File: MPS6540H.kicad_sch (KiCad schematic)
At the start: 10 parts, among them U4 MPS6540H

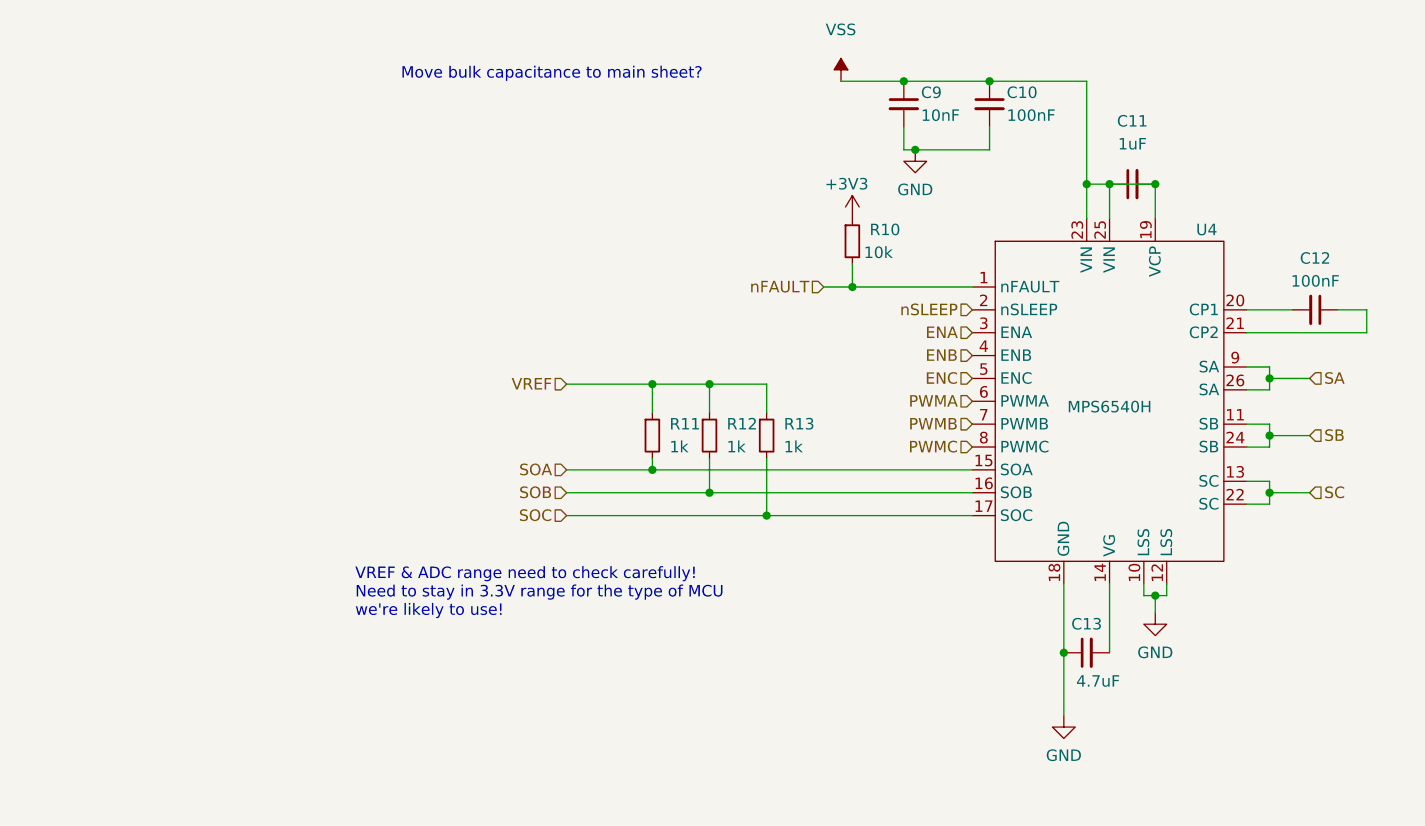
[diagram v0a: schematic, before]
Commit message: working on rosmo ESC, routing half done
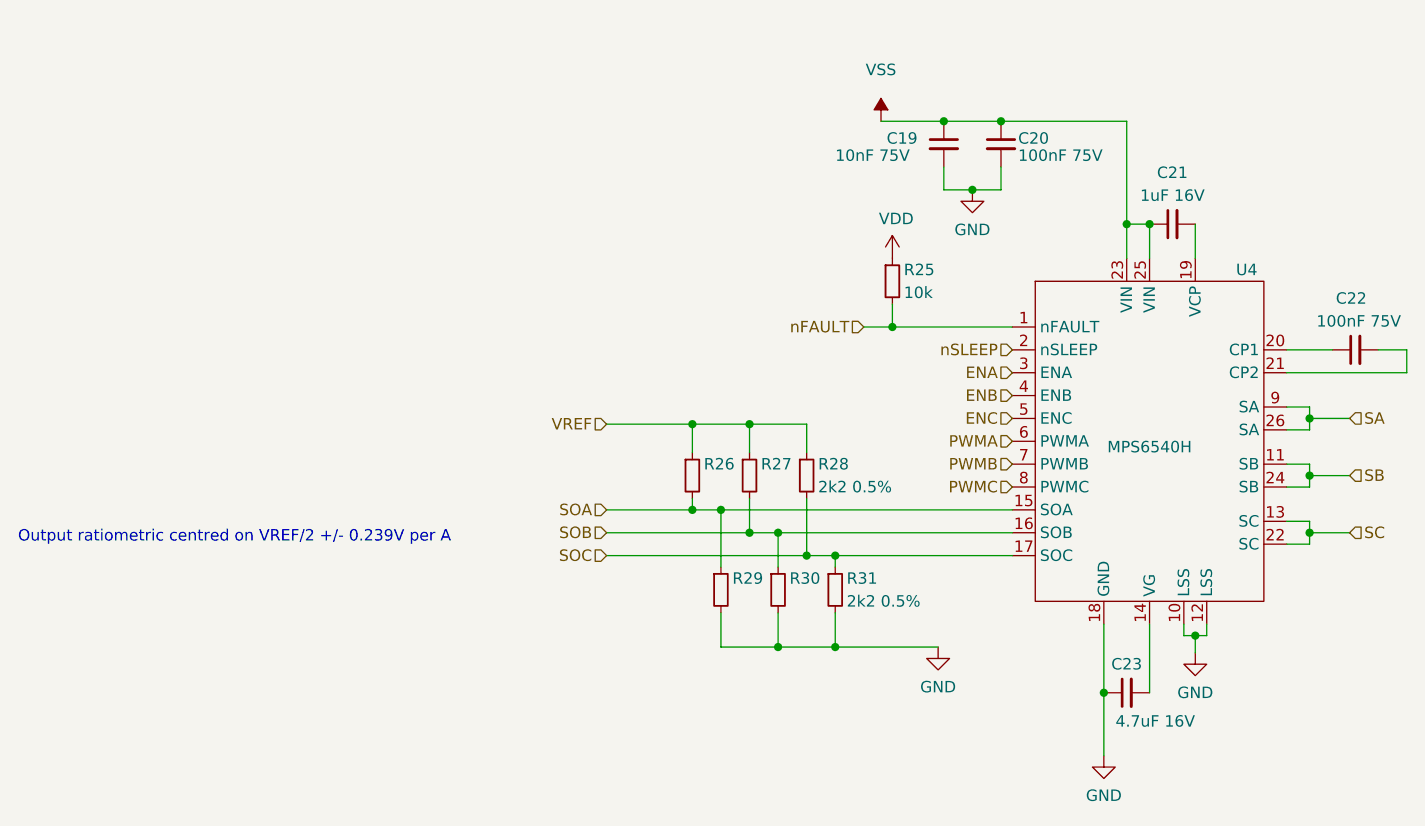
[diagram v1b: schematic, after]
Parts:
- removed C10, C12: 100nF, Capacitor_SMD:C_0805_2012Metric, symbol Device:C_Small
- removed C11: 1uF, Capacitor_SMD:C_0805_2012Metric, symbol Device:C_Small
- removed C13: 4.7uF, Capacitor_SMD:C_0805_2012Metric, symbol Device:C_Small
- removed C9: 10nF, Capacitor_SMD:C_0805_2012Metric, symbol Device:C_Small
- removed R10: 10k, Resistor_SMD:R_0402_1005Metric, symbol Device:R_Small
- removed R11, R12: 1k, Resistor_SMD:R_0402_1005Metric, symbol Device:R_Small
- removed R13: 1k, Capacitor_SMD:C_0805_2012Metric, symbol Device:R_Small
- added C19: 10nF 75V, Capacitor_SMD:C_0805_2012Metric, symbol Device:C_Small
- added C20, C22: 100nF 75V, Capacitor_SMD:C_0805_2012Metric, symbol Device:C_Small
- added C21: 1uF 16V, Capacitor_SMD:C_0603_1608Metric, symbol Device:C_Small
- added C23: 4.7uF 16V, Capacitor_SMD:C_0603_1608Metric, symbol Device:C_Small
- added R25: 10k, Resistor_SMD:R_0402_1005Metric, symbol Device:R_Small
- added R26, R27, R28, R29, R30, R31: 2k2 0.5%, Resistor_SMD:R_0402_1005Metric, symbol Device:R_Small
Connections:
- net GND: now also C19.2, C20.2, C23.1, R29.2, R30.2, R31.2
- net SOA: now also R26.2, R29.1
- net SOB: now also R27.2, R30.1
- net SOC: now also R28.2, R31.1
- net VREF: now also R26.1, R27.1, R28.1
- net VSS: now also C19.1, C20.1, C21.1; no longer U4.19 (VCP)
- net nFAULT: now also R25.2
- net at U4.14 (VG): now also C23.2
- net at U4.21 (CP2): now also C22.2
- net at U4.20 (CP1): now also C22.1
- new net: C21.2, U4.19 (VCP)
- new net VDD: R25.1
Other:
- note added: "Output ratiometric centred on VREF/2 +/- 0.239V per A"
- note removed: "Move bulk capacitance to main sheet?"
- note removed: "VREF & ADC range need to check carefully! Need to stay in 3.3V range for the type of MCU we're likely to use!"

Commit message: intial routing done
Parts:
- renumbered C19 to C14, C20 to C15, C21 to C16, C22 to C17, C23 to C18, R25 to R18, R26 to R19, R27 to R20, R28 to R21, R29 to R22, R30 to R23, R31 to R24, U4 to U3
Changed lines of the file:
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@@
   (symbol (lib_id "Device:R_Small") (at 114.3 97.79 0)
     (in_bom yes) (on_board yes)
-    (property "Reference" "R26" (id 0) (at 115.57 96.5199 0)
+    (property "Reference" "R19" (id 0) (at 115.57 96.5199 0)
       (effects (font (size 1.27 1.27)) (justify left))
     )
@@
   (symbol (lib_id "Device:R_Small") (at 117.475 110.49 0)
     (in_bom yes) (on_board yes)
-    (property "Reference" "R29" (id 0) (at 118.745 109.2199 0)
+    (property "Reference" "R22" (id 0) (at 118.745 109.2199 0)
       (effects (font (size 1.27 1.27)) (justify left))
     )
@@
   (symbol (lib_id "Device:R_Small") (at 120.65 97.79 0)
     (in_bom yes) (on_board yes)
-    (property "Reference" "R27" (id 0) (at 121.92 96.5199 0)
+    (property "Reference" "R20" (id 0) (at 121.92 96.5199 0)
       (effects (font (size 1.27 1.27)) (justify left))
     )
@@
   (symbol (lib_id "Device:R_Small") (at 123.825 110.49 0)
     (in_bom yes) (on_board yes)
-    (property "Reference" "R30" (id 0) (at 125.095 109.2199 0)
+    (property "Reference" "R23" (id 0) (at 125.095 109.2199 0)
       (effects (font (size 1.27 1.27)) (justify left))
     )
@@
   (symbol (lib_id "Device:R_Small") (at 127 97.79 0)
     (in_bom yes) (on_board yes)
-    (property "Reference" "R28" (id 0) (at 128.27 96.5199 0)
+    (property "Reference" "R21" (id 0) (at 128.27 96.5199 0)
       (effects (font (size 1.27 1.27)) (justify left))
     )
@@
   (symbol (lib_id "Device:R_Small") (at 130.175 110.49 0)
     (in_bom yes) (on_board yes)
-    (property "Reference" "R31" (id 0) (at 131.445 109.2199 0)
+    (property "Reference" "R24" (id 0) (at 131.445 109.2199 0)
       (effects (font (size 1.27 1.27)) (justify left))
     )
@@
   (symbol (lib_id "Device:R_Small") (at 136.525 76.2 0)
     (in_bom yes) (on_board yes)
-    (property "Reference" "R25" (id 0) (at 137.795 74.9299 0)
+    (property "Reference" "R18" (id 0) (at 137.795 74.9299 0)
       (effects (font (size 1.27 1.27)) (justify left))
     )
@@
   (symbol (lib_id "Device:C_Small") (at 142.24 60.96 0)
     (in_bom yes) (on_board yes)
-    (property "Reference" "C19" (id 0) (at 135.89 60.3249 0)
+    (property "Reference" "C14" (id 0) (at 135.89 60.3249 0)
       (effects (font (size 1.27 1.27)) (justify left))
     )
@@
   (symbol (lib_id "Device:C_Small") (at 148.59 60.96 0)
     (in_bom yes) (on_board yes)
-    (property "Reference" "C20" (id 0) (at 150.495 60.3249 0)
+    (property "Reference" "C15" (id 0) (at 150.495 60.3249 0)
       (effects (font (size 1.27 1.27)) (justify left))
     )
@@
   (symbol (lib_id "Device:C_Small") (at 162.56 121.92 90)
     (in_bom yes) (on_board yes)
-    (property "Reference" "C23" (id 0) (at 162.56 118.745 90))
+    (property "Reference" "C18" (id 0) (at 162.56 118.745 90))
     (property "Value" "4.7uF 16V" (id 1) (at 165.735 125.095 90))
     (property "Footprint" "Capacitor_SMD:C_0603_1608Metric" (id 2) (at 162.56 121.92 0)
@@
   (symbol (lib_id "Device:C_Small") (at 167.64 69.85 90)
     (in_bom yes) (on_board yes)
-    (property "Reference" "C21" (id 0) (at 167.64 64.135 90))
+    (property "Reference" "C16" (id 0) (at 167.64 64.135 90))
     (property "Value" "1uF 16V" (id 1) (at 167.64 66.675 90))
     (property "Footprint" "Capacitor_SMD:C_0603_1608Metric" (id 2) (at 167.64 69.85 0)
@@
   (symbol (lib_id "Device:C_Small") (at 187.96 83.82 90)
     (in_bom yes) (on_board yes)
-    (property "Reference" "C22" (id 0) (at 189.2299 78.105 90)
+    (property "Reference" "C17" (id 0) (at 189.2299 78.105 90)
       (effects (font (size 1.27 1.27)) (justify left))
     )
@@
   (symbol (lib_id "runger:MPS6540H") (at 165.1 93.98 0)
     (in_bom yes) (on_board yes)
-    (property "Reference" "U4" (id 0) (at 175.895 74.93 0))
+    (property "Reference" "U3" (id 0) (at 175.895 74.93 0))
     (property "Value" "MPS6540H" (id 1) (at 165.1 94.615 0))
     (property "Footprint" "runger:MPS6540H" (id 2) (at 149.86 81.28 0)

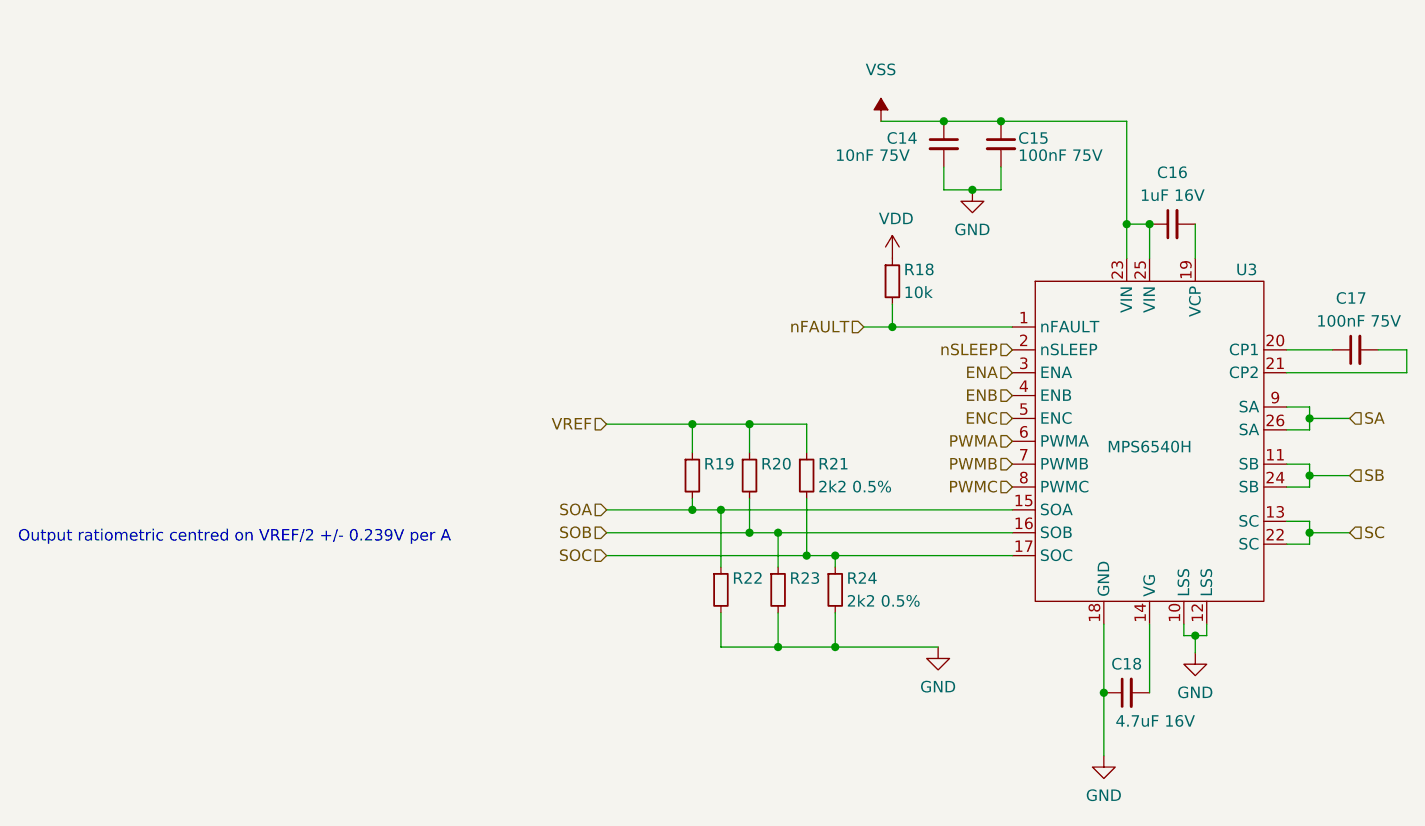
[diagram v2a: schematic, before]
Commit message: updated to KiCad 6
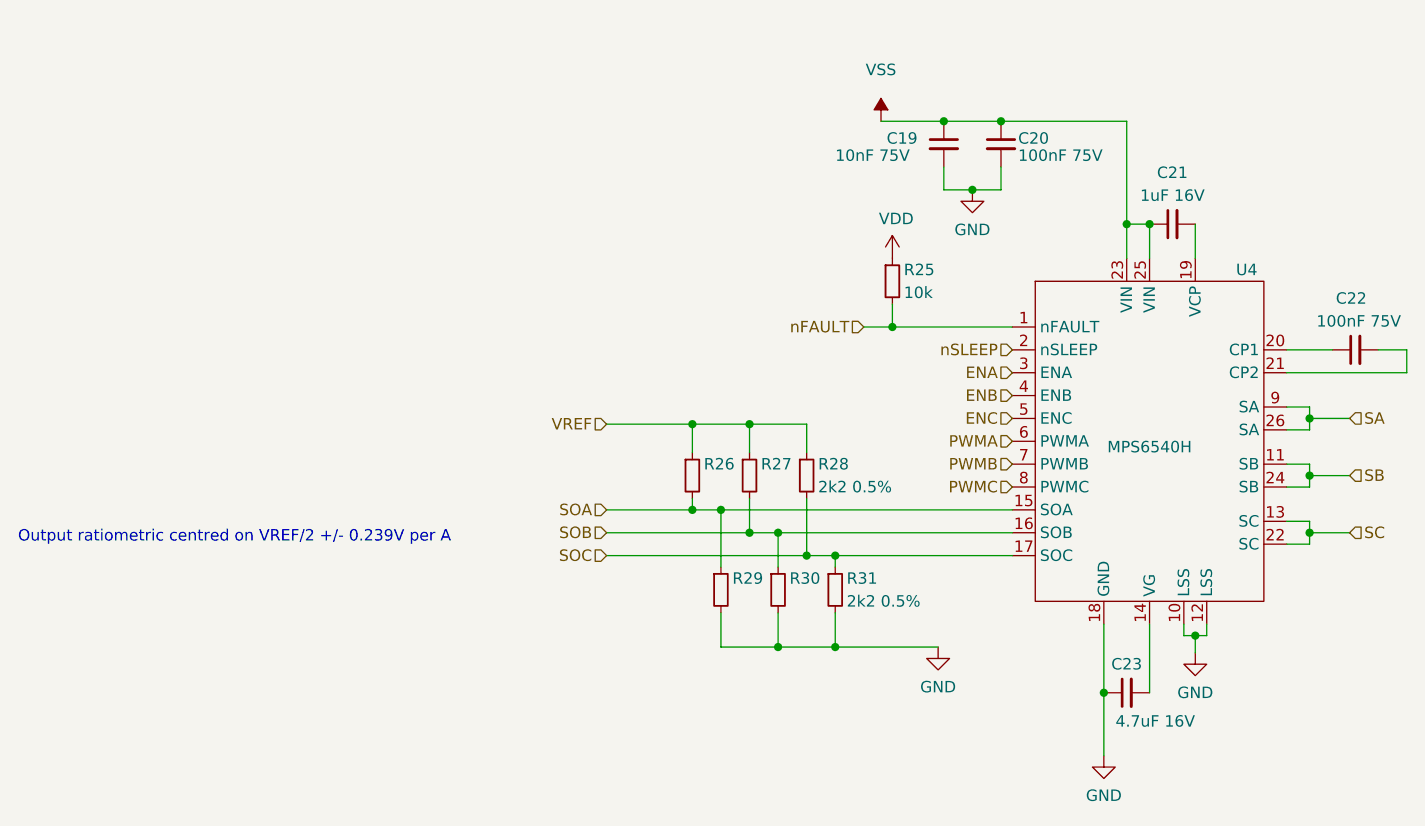
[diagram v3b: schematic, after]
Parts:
- renumbered C14 to C19, C15 to C20, C16 to C21, C17 to C22, C18 to C23, R18 to R25, R19 to R26, R20 to R27, R21 to R28, R22 to R29, R23 to R30, R24 to R31, U3 to U4

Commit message: v1 prototype for production
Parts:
- U4: Manu (none) -> Monolithic Power Systems; Part (none) -> MPS6540H
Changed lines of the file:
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@@
+      (effects (font (size 1.27 1.27)) hide)
+    )
+    (property "Manu" "Monolithic Power Systems" (id 4) (at 165.1 93.98 0)
+      (effects (font (size 1.27 1.27)) hide)
+    )
+    (property "Part" "MPS6540H" (id 5) (at 165.1 93.98 0)
       (effects (font (size 1.27 1.27)) hide)
     )
